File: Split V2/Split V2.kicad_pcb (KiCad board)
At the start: 2 copper layers, 165.9 x 121.3 mm, 67 parts, among them J1 AudioJack4

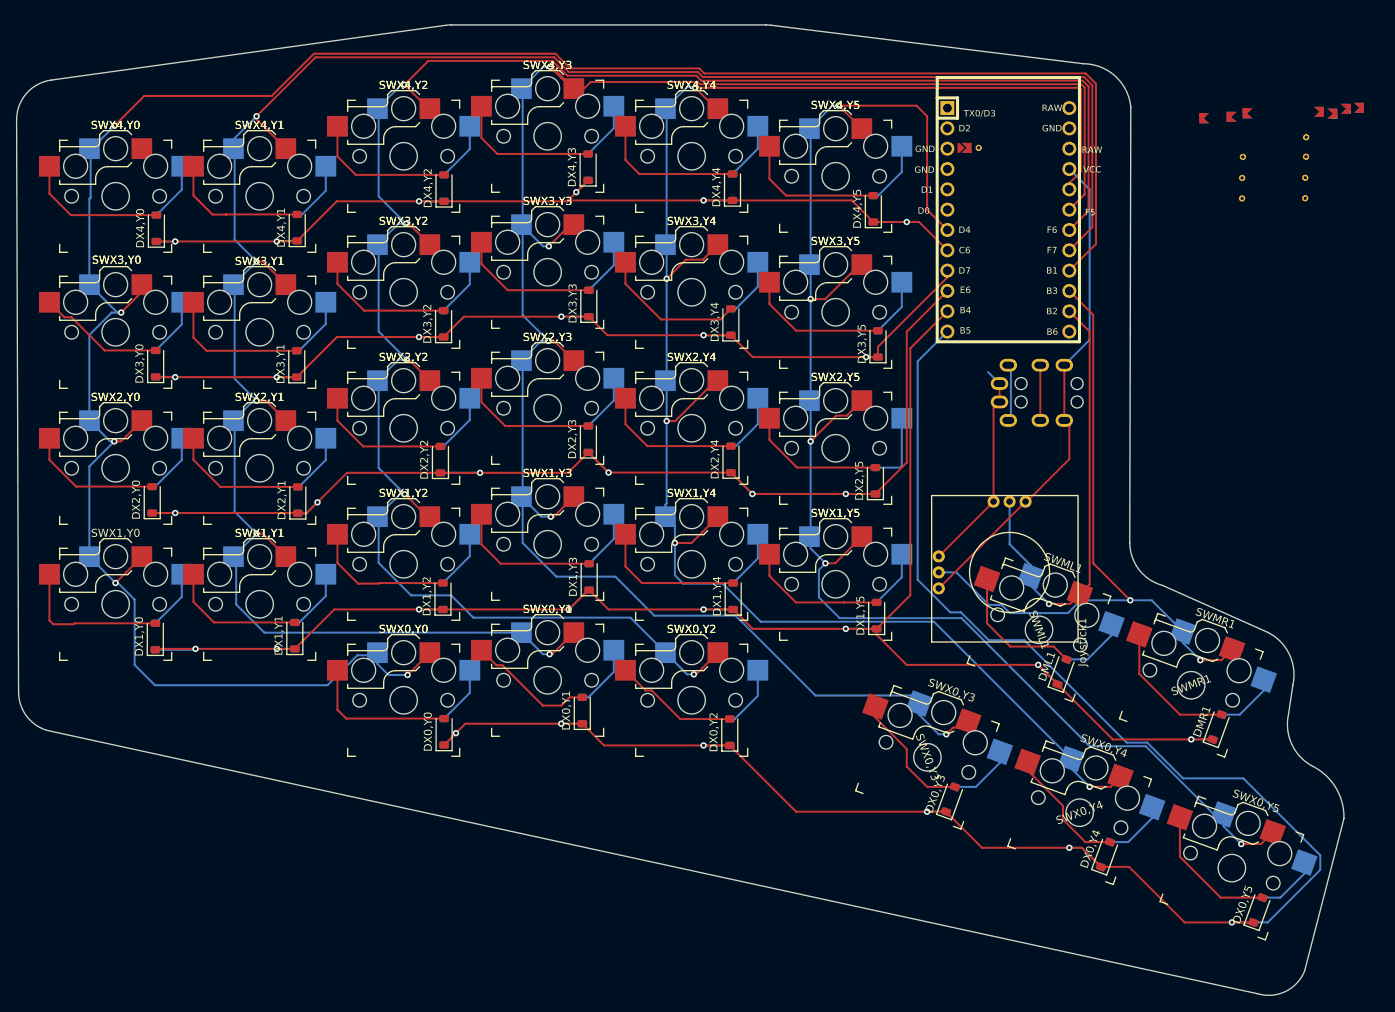
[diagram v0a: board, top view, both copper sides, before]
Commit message: Finished up double sided promicro
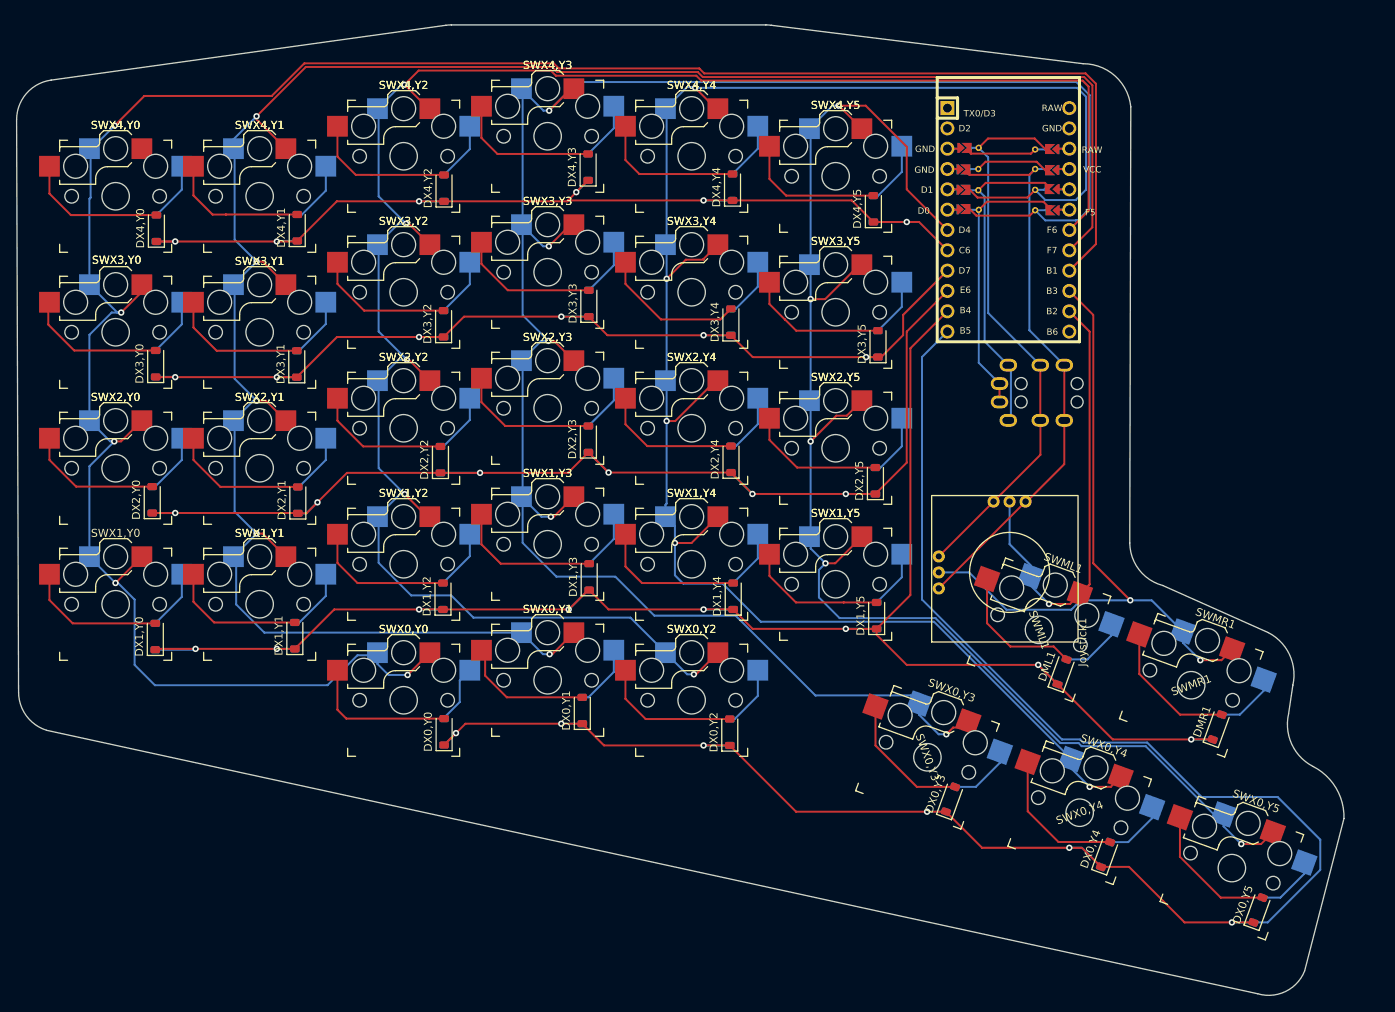
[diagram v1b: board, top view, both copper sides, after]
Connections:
- J1 pad 1: Gnd -> SCL
- J1 pad 2: SCL -> SDA
- J1 pad 3: SDA -> Gnd
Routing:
- net Gnd: track 26.8 -> 74.9 mm
- net SDA: track 6.90 -> 44.3 mm
- net SCL: track 7.17 -> 39.0 mm
- net Col4: track 220.4 -> 242.4 mm
- net Col3: track 243.2 -> 264.0 mm
- net unconnected-(ProMicro1-GND-Pad4): track 0.00 -> 14.2 mm
- net unconnected-(ProMicro1-RST-Pad22): track 0.00 -> 13.6 mm
- net VCC: track 61.9 -> 74.9 mm
- net Col5: track 191.7 -> 187.9 mm
- net Net-(DX0,Y2-A): track 23.5 -> 27.0 mm
- net Net-(DX0,Y4-A): track 24.0 -> 25.9 mm
- net Net-(DX3,Y0-A): track 23.2 -> 25.0 mm
- net Row0: track 240.6 -> 242.4 mm
- net Net-(DX1,Y0-A): track 26.8 -> 25.2 mm
- net Net-(DX2,Y5-A): track 26.8 -> 25.3 mm
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
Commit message: Mounting
Added mounting
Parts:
- added REF**: MountingHole_2.1mm, MountingHole:MountingHole_2.1mm, F.Cu at (174.9, 57.7)
- added REF**: MountingHole_2.1mm, MountingHole:MountingHole_2.1mm, F.Cu at (203.3, 85.7)
- added REF**: MountingHole_2.1mm, MountingHole:MountingHole_2.1mm, F.Cu at (218.4, 165.7)
- added REF**: MountingHole_2.1mm, MountingHole:MountingHole_2.1mm, F.Cu at (163.2, 152.4)
- added REF**: MountingHole_2.1mm, MountingHole:MountingHole_2.1mm, F.Cu at (213.4, 108.6)
- added REF**: MountingHole_2.1mm, MountingHole:MountingHole_2.1mm, F.Cu at (235.3, 147.0)
- added REF**: MountingHole_2.1mm, MountingHole:MountingHole_2.1mm, F.Cu at (86.2, 65.9)
- added REF**: MountingHole_2.1mm, MountingHole:MountingHole_2.1mm, F.Cu at (92.1, 138.4)
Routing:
- net B2: track 56.1 -> 58.4 mm

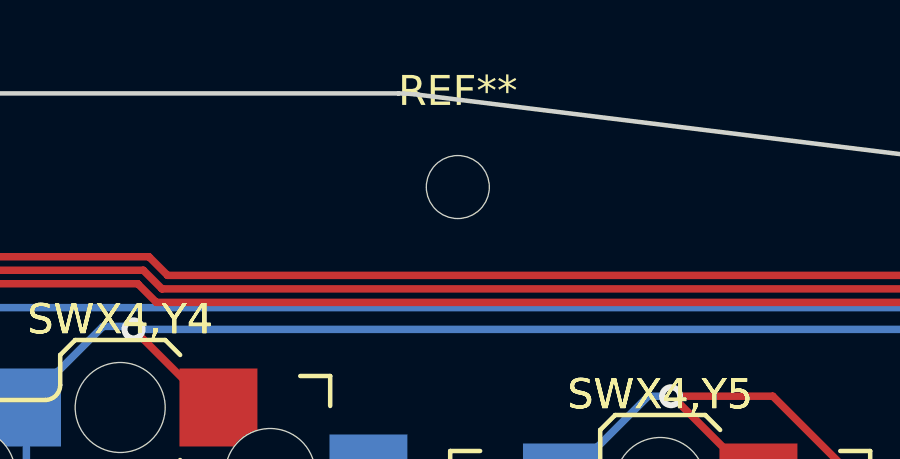
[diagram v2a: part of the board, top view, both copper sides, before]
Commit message: adjusted mounting
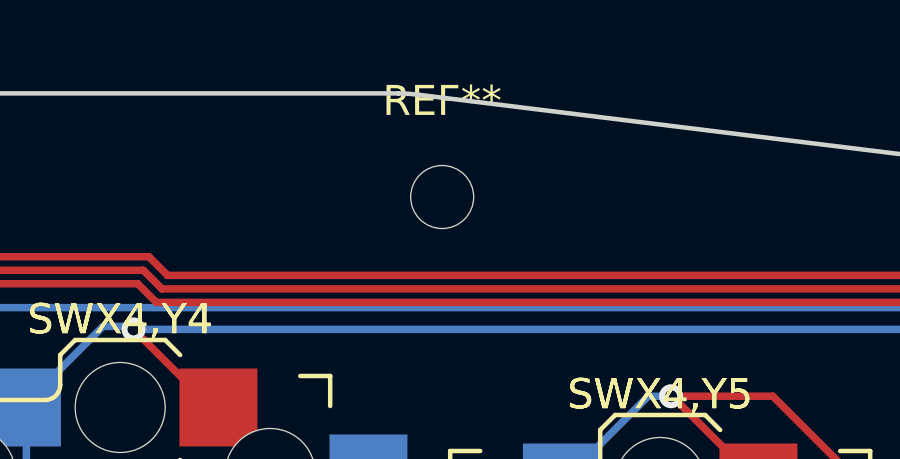
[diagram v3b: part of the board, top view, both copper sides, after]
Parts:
- moved REF** 0.62 mm to (174.3, 58.1)
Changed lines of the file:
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@@
 	(footprint "MountingHole:MountingHole_2.1mm"
 		(layer "F.Cu")
-		(at 174.864606 57.741782)
+		(at 174.342576 58.074257)
 		(descr "Mounting Hole 2.1mm, no annular")
 		(tags "mounting hole 2.1mm no annular")

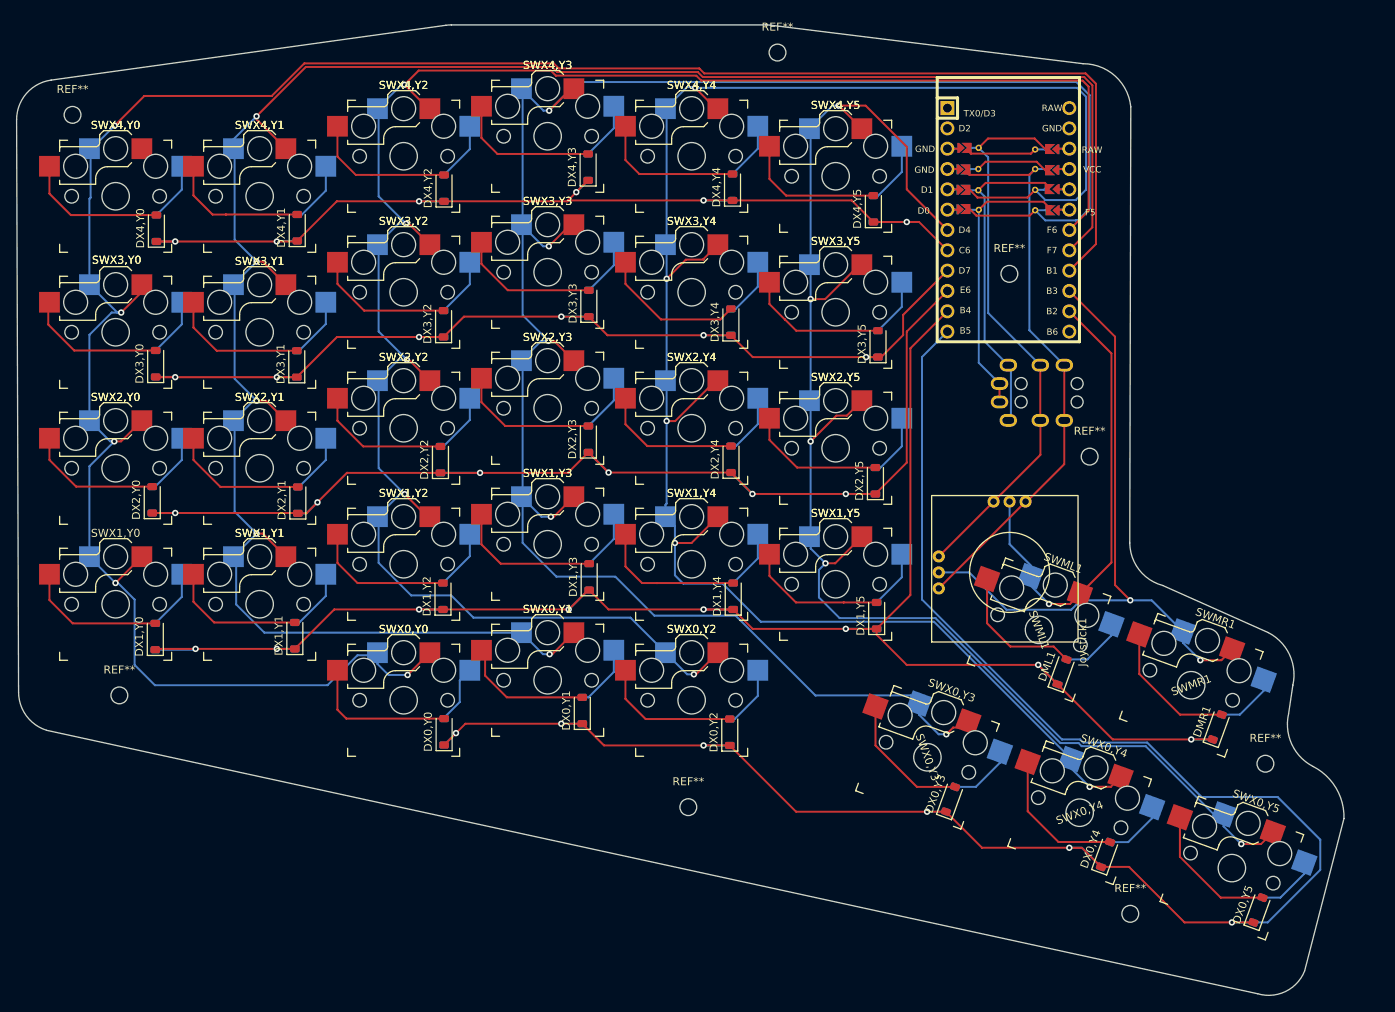
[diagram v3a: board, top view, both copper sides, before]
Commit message: Cleaned up Silkscreen
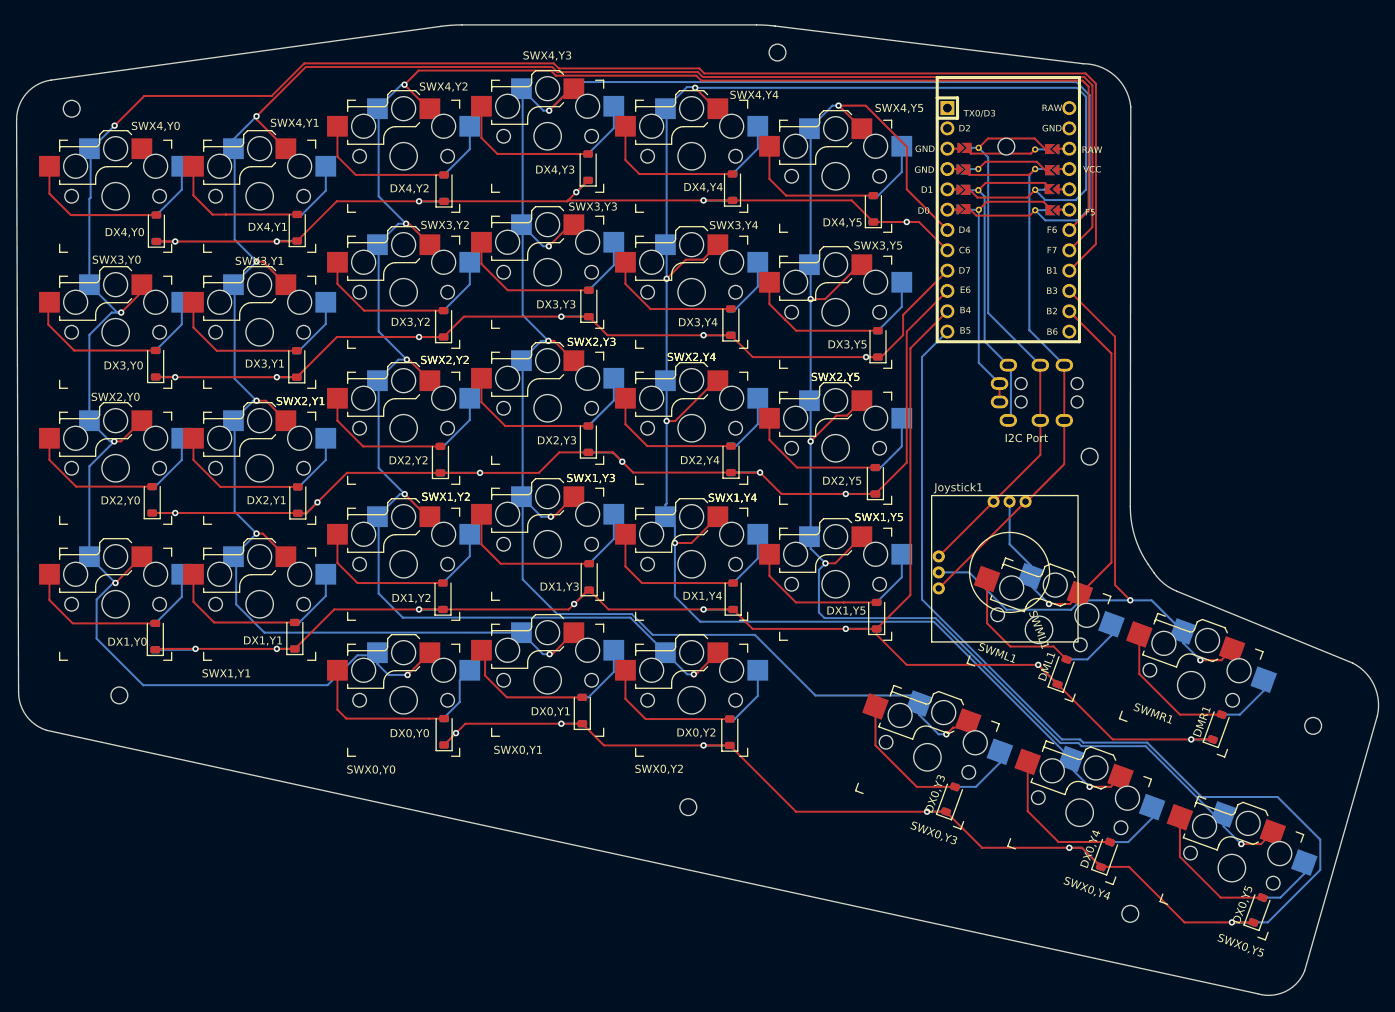
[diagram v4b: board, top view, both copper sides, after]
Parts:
- moved REF** 15.9 mm to (203.0, 69.8)
- moved REF** 7.62 mm to (241.3, 142.2)
- moved REF** 0.77 mm to (86.1, 65.1)
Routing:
- net Col0: track 287.1 -> 289.9 mm
- net Col3: track 264.0 -> 266.6 mm
- net Col2: track 243.9 -> 246.1 mm
- net Col4: track 242.4 -> 244.0 mm
- net Col5: track 187.9 -> 189.0 mm
- net Net-(DX3,Y4-A): track 25.8 -> 24.8 mm
- net Row2: track 146.7 -> 147.7 mm
- net Row1: track 214.3 -> 213.4 mm
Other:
- board size 165.9 x 121.3 mm -> 170.2 x 121.3 mm
- board text added: "Joystick1"

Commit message: silkscreen work
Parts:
- moved REF** 5.24 mm to (204.2, 64.7)
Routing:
- net Row0: track 242.4 -> 241.6 mm

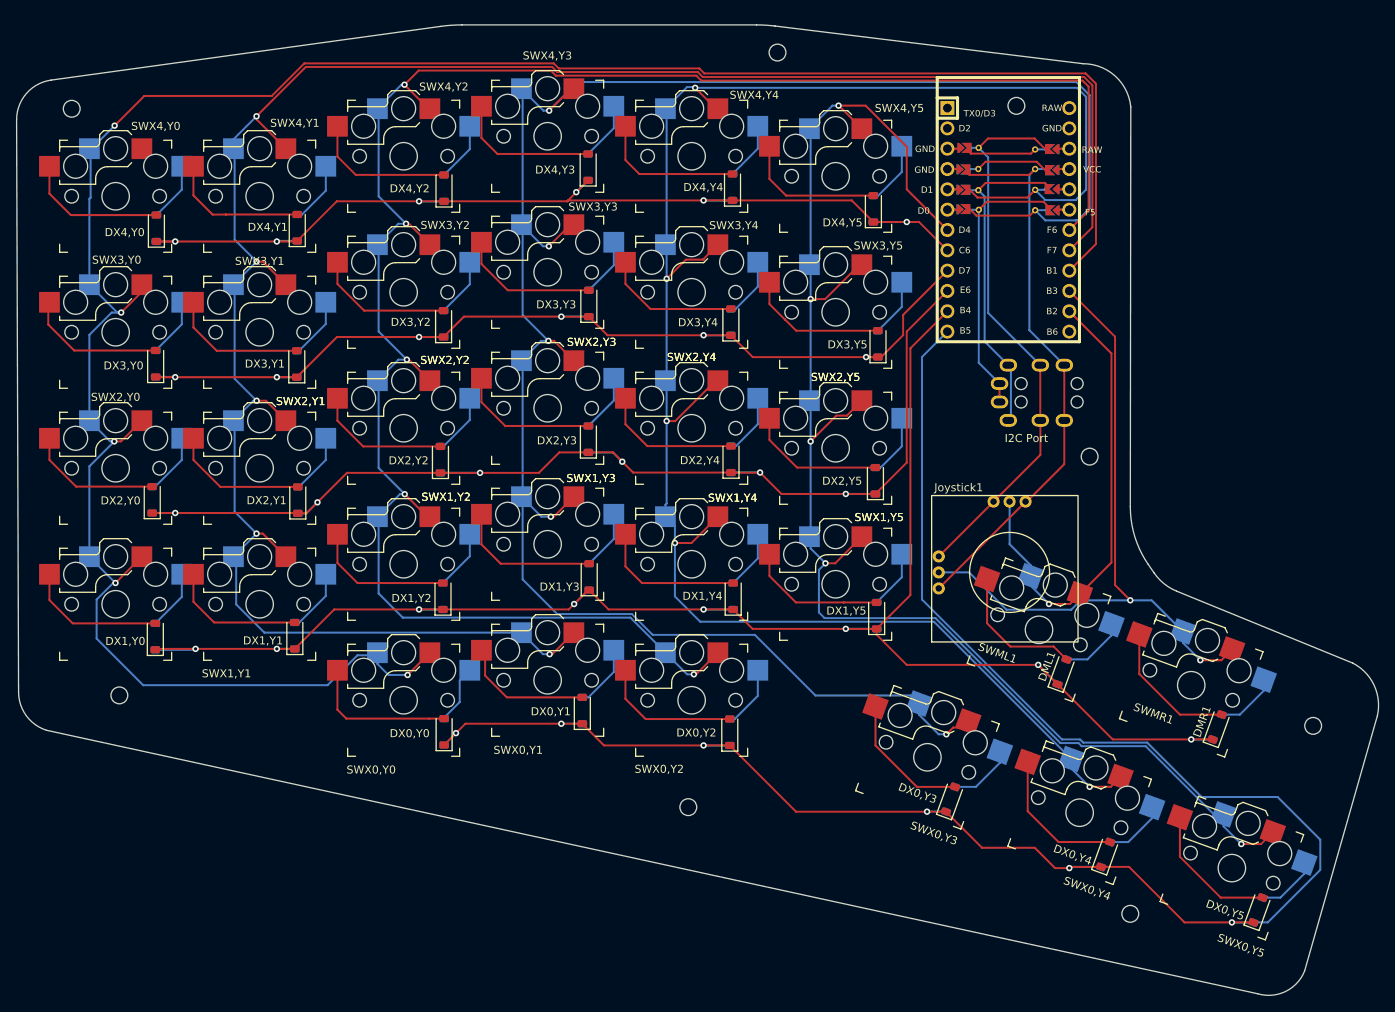
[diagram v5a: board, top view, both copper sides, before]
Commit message: moved ttrs outlet
not close enough to board edge
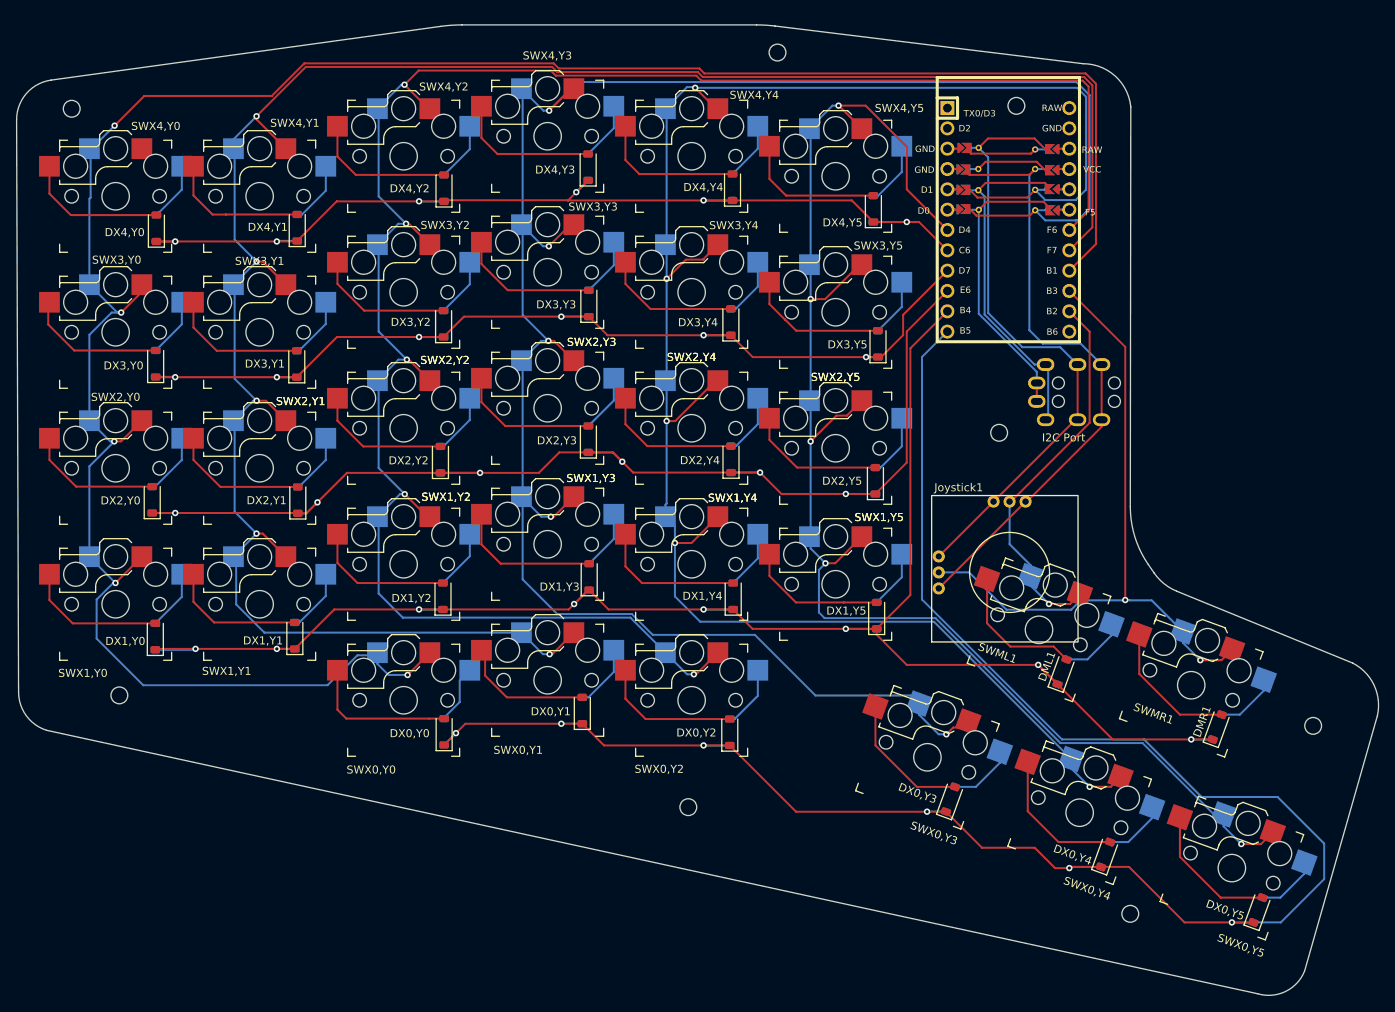
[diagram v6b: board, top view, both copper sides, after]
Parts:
- moved REF** 11.7 mm to (202.0, 105.6)
- moved J1 4.66 mm to (218.1, 101.7)
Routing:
- net B2: track 58.4 -> 48.3 mm
- net Gnd: track 74.9 -> 81.7 mm
- net VCC: track 74.9 -> 81.6 mm
- net SDA: track 44.3 -> 46.9 mm
- net SCL: track 39.0 -> 40.9 mm
- net Row0: track 241.6 -> 243.0 mm

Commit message: Final adjustments made
sent Gerber and drill files to jrcpcb
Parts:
- moved REF** 1.34 mm to (217.9, 167.0)
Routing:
- net B3: track 85.1 -> 119.2 mm, vias 2 -> 1
- net Row0: track 243.0 -> 212.2 mm
- net Col0: track 289.9 -> 294.5 mm
- net Row1: track 213.4 -> 217.6 mm
- net Col4: track 244.0 -> 248.0 mm
- net Col5: track 189.0 -> 190.7 mm
